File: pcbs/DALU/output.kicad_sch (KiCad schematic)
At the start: 8 parts, among them U801 74HC74, U802 74HCT574

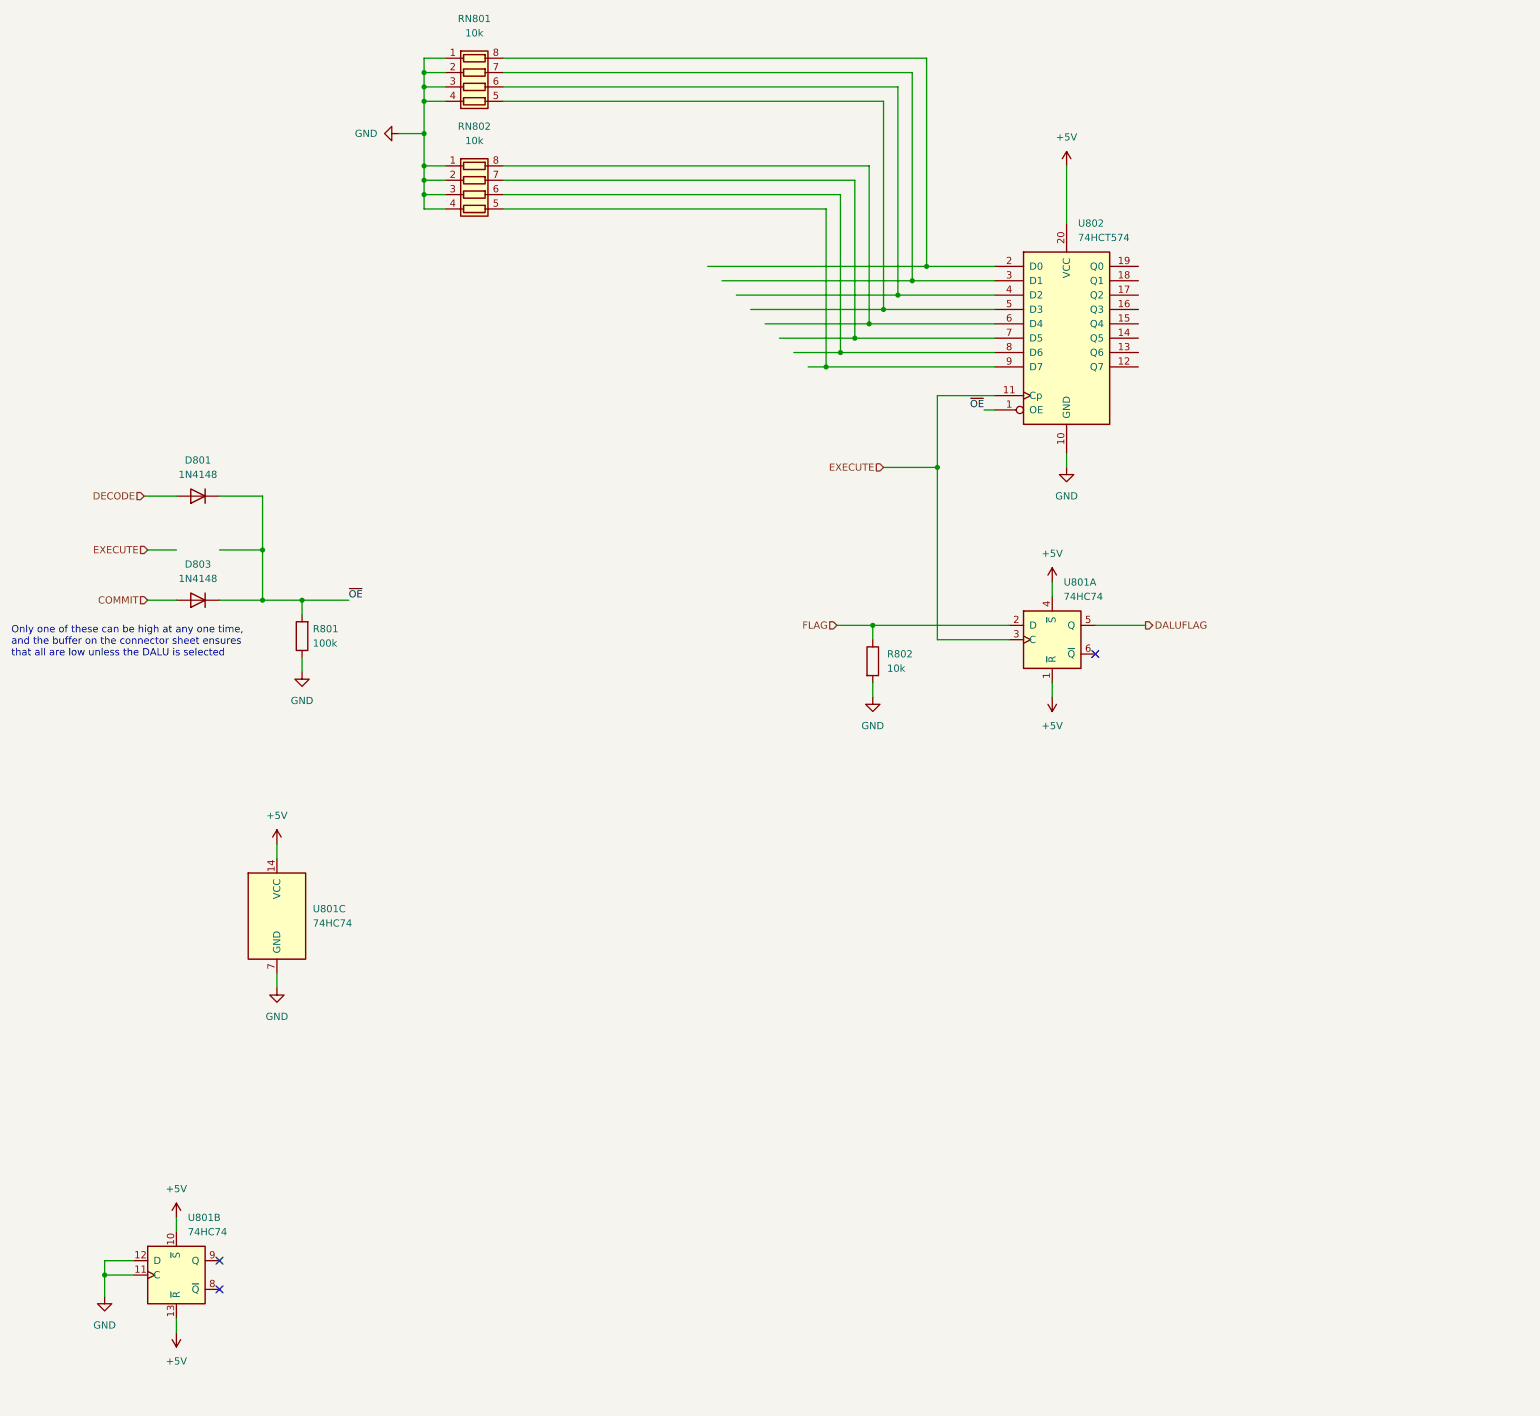
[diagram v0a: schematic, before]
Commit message: Separate out AND stage
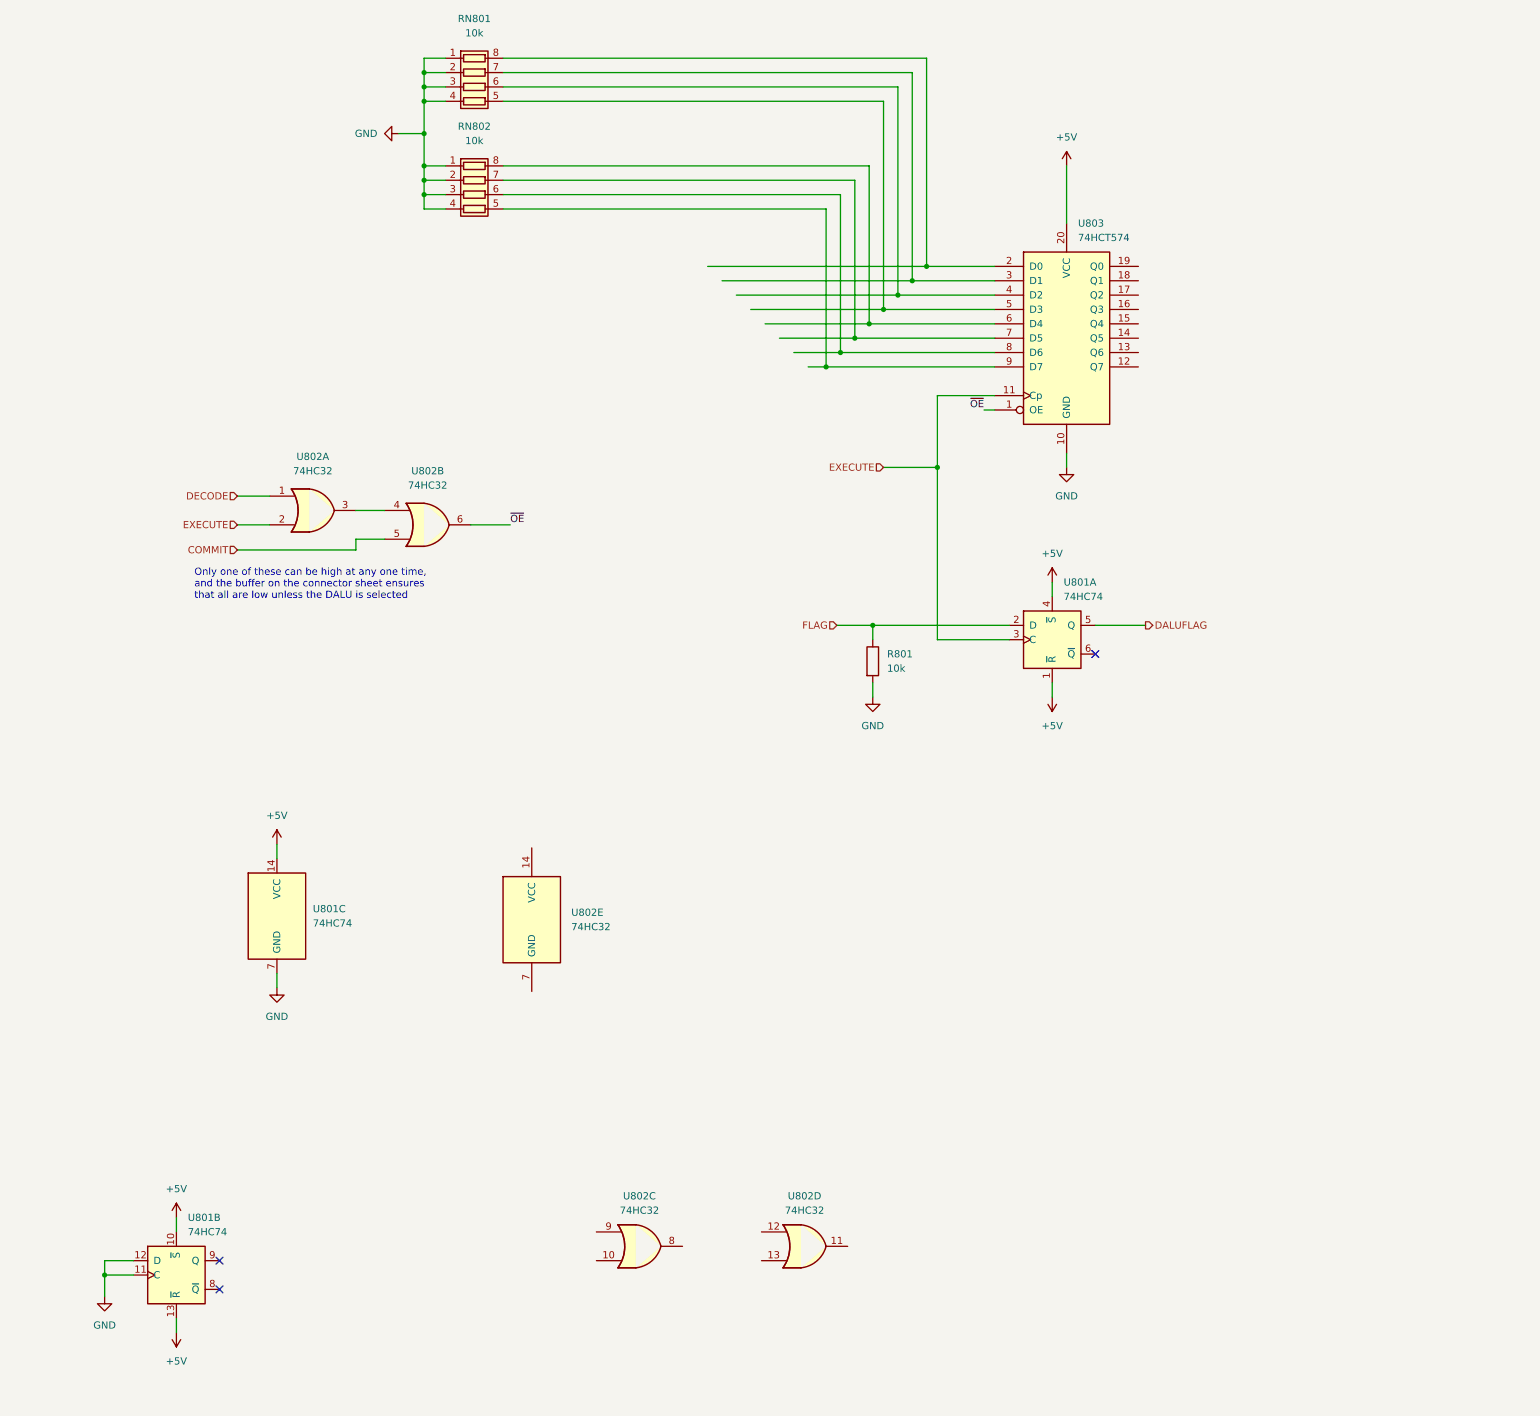
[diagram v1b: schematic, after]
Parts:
- removed D801, D803: 1N4148, Diode_THT:D_DO-35_SOD27_P7.62mm_Horizontal, symbol Diode:1N4148
- removed R801: 100k, Resistor_THT:R_Axial_DIN0207_L6.3mm_D2.5mm_P7.62mm_Horizontal, symbol Device:R
- added U802: 74HC32, Package_DIP:DIP-14_W7.62mm_Socket, symbol 74xx:74LS32
- renumbered R802 to R801, U802 to U803
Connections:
- net COMMIT: now also U802.5
- net DECODE: now also U802.1
- net EXECUTE: now also U802.2
- net ~{OE}: now also U802.6
- new net: U802.3, U802.4

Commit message: More rerouting
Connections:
- net RESULT7: now reaches RN802.5 (R4.2), U803.9 (D7)
- net RESULT6: now reaches RN802.6 (R3.2), U803.8 (D6)
- net RESULT5: now reaches RN802.7 (R2.2), U803.7 (D5)
- net RESULT4: now reaches RN802.8 (R1.2), U803.6 (D4)
- net RESULT0: now reaches RN801.8 (R1.2), U803.2 (D0)
- net RESULT1: now reaches RN801.7 (R2.2), U803.3 (D1)
- net RESULT2: now reaches RN801.6 (R3.2), U803.4 (D2)
- net RESULT3: now reaches RN801.5 (R4.2), U803.5 (D3)
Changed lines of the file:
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@@
   (no_connect (at 208.28 126.365))
   (no_connect (at 53.34 238.76))
+  (bus_entry (at 130.175 60.325) (size 2.54 2.54)
+    (stroke (width 0) (type default) (color 0 0 0 0))
+  )
+  (bus_entry (at 130.175 73.025) (size 2.54 2.54)
+    (stroke (width 0) (type default) (color 0 0 0 0))
+  )
+  (bus_entry (at 130.175 57.785) (size 2.54 2.54)
+    (stroke (width 0) (type default) (color 0 0 0 0))
+  )
+  (bus_entry (at 130.175 70.485) (size 2.54 2.54)
+    (stroke (width 0) (type default) (color 0 0 0 0))
+  )
+  (bus_entry (at 130.175 62.865) (size 2.54 2.54)
+    (stroke (width 0) (type default) (color 0 0 0 0))
+  )
+  (bus_entry (at 130.175 55.245) (size 2.54 2.54)
+    (stroke (width 0) (type default) (color 0 0 0 0))
+  )
+  (bus_entry (at 130.175 65.405) (size 2.54 2.54)
+    (stroke (width 0) (type default) (color 0 0 0 0))
+  )
+  (bus_entry (at 130.175 67.945) (size 2.54 2.54)
+    (stroke (width 0) (type default) (color 0 0 0 0))
+  )
   (wire (pts (xy 175.895 23.495) (xy 175.895 60.325))
     (stroke (width 0) (type default) (color 0 0 0 0))
@@
     (stroke (width 0) (type default) (color 0 0 0 0))
   )
-  (wire (pts (xy 175.895 60.325) (xy 142.24 60.325))
+  (wire (pts (xy 132.715 60.325) (xy 175.895 60.325))
     (stroke (width 0) (type default) (color 0 0 0 0))
   )
@@
     (stroke (width 0) (type default) (color 0 0 0 0))
   )
+  (bus (pts (xy 130.175 52.705) (xy 130.175 55.245))
+    (stroke (width 0) (type default) (color 0 0 0 0))
+  )
   (wire (pts (xy 33.02 236.22) (xy 38.1 236.22))
     (stroke (width 0) (type default) (color 0 0 0 0))
   )
+  (wire (pts (xy 132.715 75.565) (xy 160.655 75.565))
+    (stroke (width 0) (type default) (color 0 0 0 0))
+  )
   (wire (pts (xy 103.505 47.625) (xy 160.655 47.625))
     (stroke (width 0) (type default) (color 0 0 0 0))
@@
     (stroke (width 0) (type default) (color 0 0 0 0))
   )
+  (bus (pts (xy 130.175 65.405) (xy 130.175 67.945))
+    (stroke (width 0) (type default) (color 0 0 0 0))
+  )
   (wire (pts (xy 56.515 103.505) (xy 62.23 103.505))
     (stroke (width 0) (type default) (color 0 0 0 0))
@@
     (stroke (width 0) (type default) (color 0 0 0 0))
   )
-  (wire (pts (xy 173.355 62.865) (xy 144.78 62.865))
+  (wire (pts (xy 132.715 62.865) (xy 173.355 62.865))
     (stroke (width 0) (type default) (color 0 0 0 0))
   )
@@
     (stroke (width 0) (type default) (color 0 0 0 0))
   )
-  (wire (pts (xy 163.195 73.025) (xy 154.94 73.025))
+  (wire (pts (xy 132.715 73.025) (xy 163.195 73.025))
+    (stroke (width 0) (type default) (color 0 0 0 0))
+  )
+  (bus (pts (xy 130.175 62.865) (xy 130.175 65.405))
     (stroke (width 0) (type default) (color 0 0 0 0))
   )
@@
     (stroke (width 0) (type default) (color 0 0 0 0))
   )
+  (bus (pts (xy 130.175 55.245) (xy 130.175 57.785))
+    (stroke (width 0) (type default) (color 0 0 0 0))
+  )
   (wire (pts (xy 180.34 80.645) (xy 180.34 93.345))
     (stroke (width 0) (type default) (color 0 0 0 0))
@@
     (stroke (width 0) (type default) (color 0 0 0 0))
   )
-  (wire (pts (xy 165.735 70.485) (xy 152.4 70.485))
+  (wire (pts (xy 132.715 70.485) (xy 165.735 70.485))
+    (stroke (width 0) (type default) (color 0 0 0 0))
+  )
+  (bus (pts (xy 130.175 60.325) (xy 130.175 62.865))
     (stroke (width 0) (type default) (color 0 0 0 0))
   )
@@
     (stroke (width 0) (type default) (color 0 0 0 0))
   )
-  (wire (pts (xy 157.48 75.565) (xy 160.655 75.565))
-    (stroke (width 0) (type default) (color 0 0 0 0))
-  )
   (wire (pts (xy 103.505 42.545) (xy 165.735 42.545))
     (stroke (width 0) (type default) (color 0 0 0 0))
@@
     (stroke (width 0) (type default) (color 0 0 0 0))
   )
-  (wire (pts (xy 170.815 65.405) (xy 147.32 65.405))
+  (wire (pts (xy 132.715 65.405) (xy 170.815 65.405))
     (stroke (width 0) (type default) (color 0 0 0 0))
   )
@@
     (stroke (width 0) (type default) (color 0 0 0 0))
   )
-  (wire (pts (xy 178.435 57.785) (xy 139.7 57.785))
+  (wire (pts (xy 132.715 57.785) (xy 178.435 57.785))
     (stroke (width 0) (type default) (color 0 0 0 0))
   )
@@
     (stroke (width 0) (type default) (color 0 0 0 0))
   )
+  (bus (pts (xy 130.175 70.485) (xy 130.175 73.025))
+    (stroke (width 0) (type default) (color 0 0 0 0))
+  )
   (wire (pts (xy 168.275 40.005) (xy 168.275 67.945))
     (stroke (width 0) (type default) (color 0 0 0 0))
@@
     (stroke (width 0) (type default) (color 0 0 0 0))
   )
-  (wire (pts (xy 168.275 67.945) (xy 149.86 67.945))
+  (wire (pts (xy 132.715 67.945) (xy 168.275 67.945))
+    (stroke (width 0) (type default) (color 0 0 0 0))
+  )
+  (bus (pts (xy 128.905 52.705) (xy 130.175 52.705))
     (stroke (width 0) (type default) (color 0 0 0 0))
   )
@@
     (stroke (width 0) (type default) (color 0 0 0 0))
   )
+  (bus (pts (xy 130.175 67.945) (xy 130.175 70.485))
+    (stroke (width 0) (type default) (color 0 0 0 0))
+  )
   (wire (pts (xy 45.72 226.06) (xy 45.72 228.6))
     (stroke (width 0) (type default) (color 0 0 0 0))
@@
   )
   (wire (pts (xy 89.535 23.495) (xy 89.535 26.035))
+    (stroke (width 0) (type default) (color 0 0 0 0))
+  )
+  (bus (pts (xy 130.175 57.785) (xy 130.175 60.325))
     (stroke (width 0) (type default) (color 0 0 0 0))
   )
@@
     (effects (font (size 1.27 1.27)) (justify right bottom))
   )
+  (label "RESULT7" (at 132.715 75.565 0)
+    (effects (font (size 1.27 1.27)) (justify left bottom))
+  )
+  (label "RESULT4" (at 132.715 67.945 0)
+    (effects (font (size 1.27 1.27)) (justify left bottom))
+  )
+  (label "RESULT3" (at 132.715 65.405 0)
+    (effects (font (size 1.27 1.27)) (justify left bottom))
+  )
   (label "~{OE}" (at 104.775 103.505 0)
+    (effects (font (size 1.27 1.27)) (justify left bottom))
+  )
+  (label "RESULT5" (at 132.715 70.485 0)
+    (effects (font (size 1.27 1.27)) (justify left bottom))
+  )
+  (label "RESULT2" (at 132.715 62.865 0)
+    (effects (font (size 1.27 1.27)) (justify left bottom))
+  )
+  (label "RESULT0" (at 132.715 57.785 0)
+    (effects (font (size 1.27 1.27)) (justify left bottom))
+  )
+  (label "RESULT6" (at 132.715 73.025 0)
+    (effects (font (size 1.27 1.27)) (justify left bottom))
+  )
+  (label "RESULT1" (at 132.715 60.325 0)
     (effects (font (size 1.27 1.27)) (justify left bottom))
   )
@@
     (effects (font (size 1.27 1.27)) (justify right))
   )
+  (hierarchical_label "RESULT[0..7]" (shape input) (at 128.905 52.705 180)
+    (effects (font (size 1.27 1.27)) (justify right))
+  )
